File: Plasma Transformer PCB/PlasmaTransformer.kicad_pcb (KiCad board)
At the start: 2 copper layers, 90 x 90 mm, 86 parts, among them J1 Barrel_Jack_MountingPin, J10 Conn_01x01_Socket, J11 Screw_Terminal_01x01, J12 Screw_Terminal_01x01, J13 Conn_01x01_Socket, J14 Conn_01x01_Socket, J15 Conn_01x01_Socket, J16 Conn_01x01_Socket, J17 Conn_01x01_Socket, J18 Conn_01x01_Socket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

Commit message: WIP rev
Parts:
- removed H2: MountingHole, MountingHole:MountingHole_8.4mm_M8
- removed HS1: Heatsink, Library:Heatsink_75x37.5mm_Fischer_SK-594-37.5-AL
- added C31: 1nF, Capacitor_SMD:C_0805_2012Metric, F.Cu at (102.5, 49.5)
- added R11: 0.05, Resistor_SMD:R_2512_6332Metric, F.Cu at (132.5, 59.0)
- added R14: 1k, Resistor_SMD:R_0805_2012Metric, F.Cu at (98.1, 44.9)
- added R15: 1k, Resistor_SMD:R_0805_2012Metric, F.Cu at (98.1, 47.8)
- added U2: LM358, Package_TO_SOT_SMD:SOT-23-8, F.Cu at (102.9, 45.8)
- C10, C5, C6, C7, C8, C9: footprint Capacitor_SMD:C_1812_4532Metric -> Capacitor_SMD:C_1206_3216Metric
- C11, C12, C21: footprint Capacitor_SMD:C_1812_4532Metric -> Capacitor_SMD:C_0805_2012Metric
- C3: value 2.7nF -> 3.3nF; footprint Capacitor_SMD:C_1812_4532Metric -> Capacitor_SMD:C_1206_3216Metric
- C4: value 1.8nF -> 3.3nF; footprint Capacitor_SMD:C_1812_4532Metric -> Capacitor_SMD:C_1206_3216Metric
- H1: value MountingHole_Pad -> Pad_Doorknob_Cap
- Q1: footprint Package_TO_SOT_THT:TO-247-3_Horizontal_TabDown -> Package_TO_SOT_SMD:Infineon_PG-HSOF-8-2_ThermalVias
- moved D2 35.0 mm to (105.6, 72.0), turned to 180 degrees
- moved J4 22.2 mm to (122.8, 102.0), turned to 0 degrees
- moved Q1 20.2 mm to (104.6, 82.7), turned to -90 degrees
- moved C11 19.3 mm to (87.2, 58.5), turned to 180 degrees
- moved R5 18.3 mm to (87.2, 60.5), turned to 0 degrees
- moved J2 15.9 mm to (141.5, 86.8)
- moved C21 15.6 mm to (61.3, 70.0), turned to 90 degrees
- moved C7 15.1 mm to (114.6, 105.8), turned to 180 degrees
- moved R2 15.0 mm to (92.6, 56.5), turned to 180 degrees
- moved C2 15.0 mm to (136.0, 72.0), turned to 90 degrees
- moved RV1 13.8 mm to (83.0, 60.0)
- moved R4 13.3 mm to (87.2, 62.5), turned to 0 degrees
- moved J1 12.5 mm to (112.0, 67.0)
- moved SW1 12.5 mm to (124.0, 73.5)
- moved L3 11.8 mm to (139.0, 101.0)
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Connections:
- J1 pad 2: GND -> /GND-IN
- Q1 pad 2: /DRAIN -> GND
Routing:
- net /DRAIN: track 83.2 -> 1.59 mm
- net /GATE: track 70.7 -> 150.3 mm, vias 0 -> 2
- net Net-(C11-Pad2): track 54.7 -> 8.39 mm
- net /VIN: track 14.1 -> 0.00 mm
- net GND: track 21.2 -> 10.7 mm, vias 14 -> 12
- net Net-(J4-Pin_1): track 12.1 -> 4.22 mm
- net Net-(J4-Pin_5): track 11.3 -> 4.23 mm
- net Net-(J4-Pin_3): track 11.3 -> 4.25 mm
- net Net-(J3-In): track 11.9 -> 5.81 mm
- net Net-(J4-Pin_7): track 9.95 -> 4.23 mm
- net Net-(C21-Pad1): track 5.28 -> 10.3 mm
- net Net-(R4-Pad1): track 8.42 -> 4.32 mm
- net Net-(C21-Pad2): track 6.83 -> 3.35 mm
- net Net-(U1-CB): track 3.96 -> 0.73 mm
- net Net-(J6-Pin_8): track 7.72 -> 5.03 mm
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- added copper zone on F.Cu, net /GND-IN
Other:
- board text added: "REV 6 | NOV 2025 | E. CHIU"
- board text removed: "REV 5 | OCT 2025 E. CHIU"

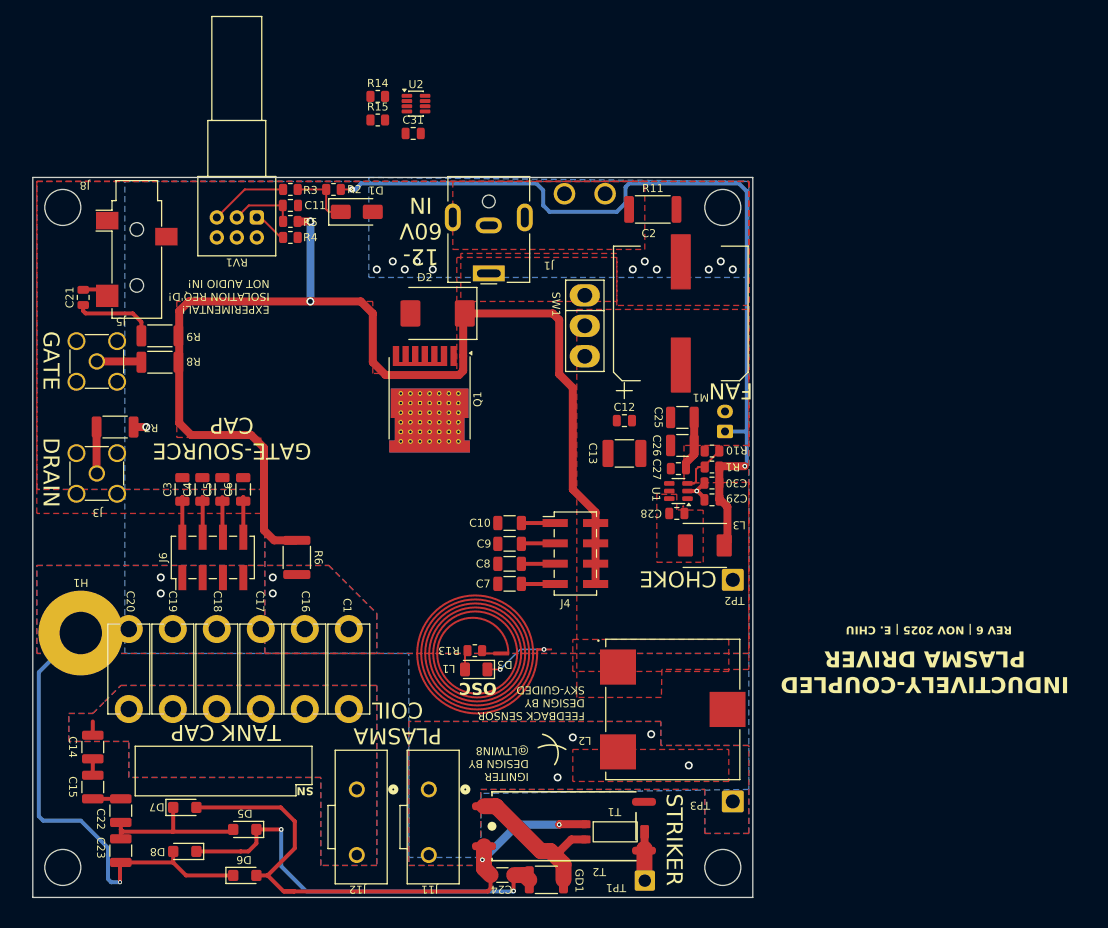
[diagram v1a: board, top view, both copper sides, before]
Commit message: mounting holes and silkscreens
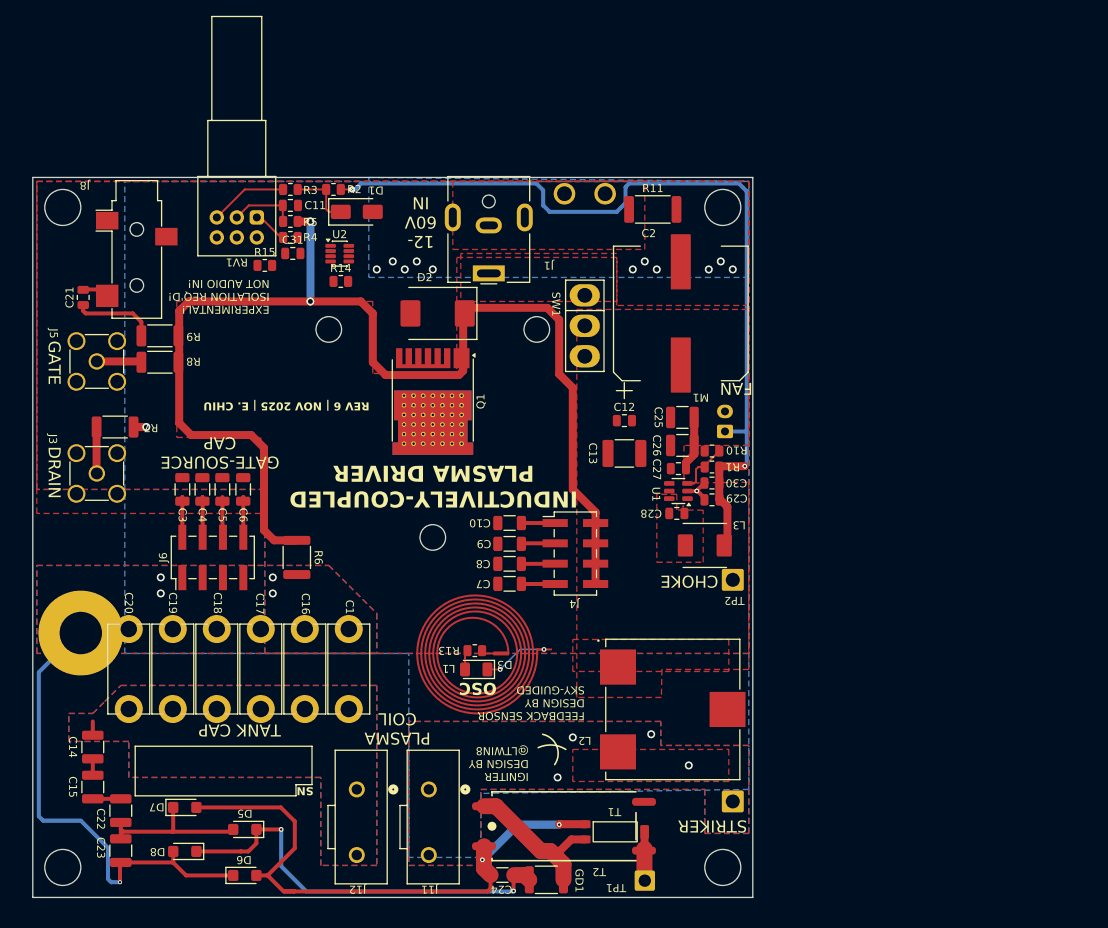
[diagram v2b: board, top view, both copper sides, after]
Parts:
- added H2: MountingHole, MountingHole:MountingHole_3.2mm_M3, F.Cu at (92.0, 74.0)
- added H3: MountingHole, MountingHole:MountingHole_3.2mm_M3, F.Cu at (118.0, 74.0)
- added H4: MountingHole, MountingHole:MountingHole_3.2mm_M3, F.Cu at (105.0, 100.0)
- Q1: footprint Package_TO_SOT_SMD:Infineon_PG-HSOF-8-2_ThermalVias -> ALibrary:IMT40R025M2HXTMA1
- moved R14 23.6 mm to (93.5, 68.0)
- moved R15 23.0 mm to (84.0, 66.0)
- moved C31 21.2 mm to (87.5, 64.5)
- moved U2 21.0 mm to (93.4, 64.5)
- moved Q1 0.49 mm to (105.0, 83.0)
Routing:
- net /GATE: track 150.3 -> 150.9 mm
